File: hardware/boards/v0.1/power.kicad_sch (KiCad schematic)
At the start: 69 parts, among them IC3 SP3401-02UTG, J2 USB, U20 TPS62A02ADRLR, U23 FUSB302BxxMPX, U36 STM6601GU2BDM6F, U39 BQ27531YZFR-G1, U45 BQ24193

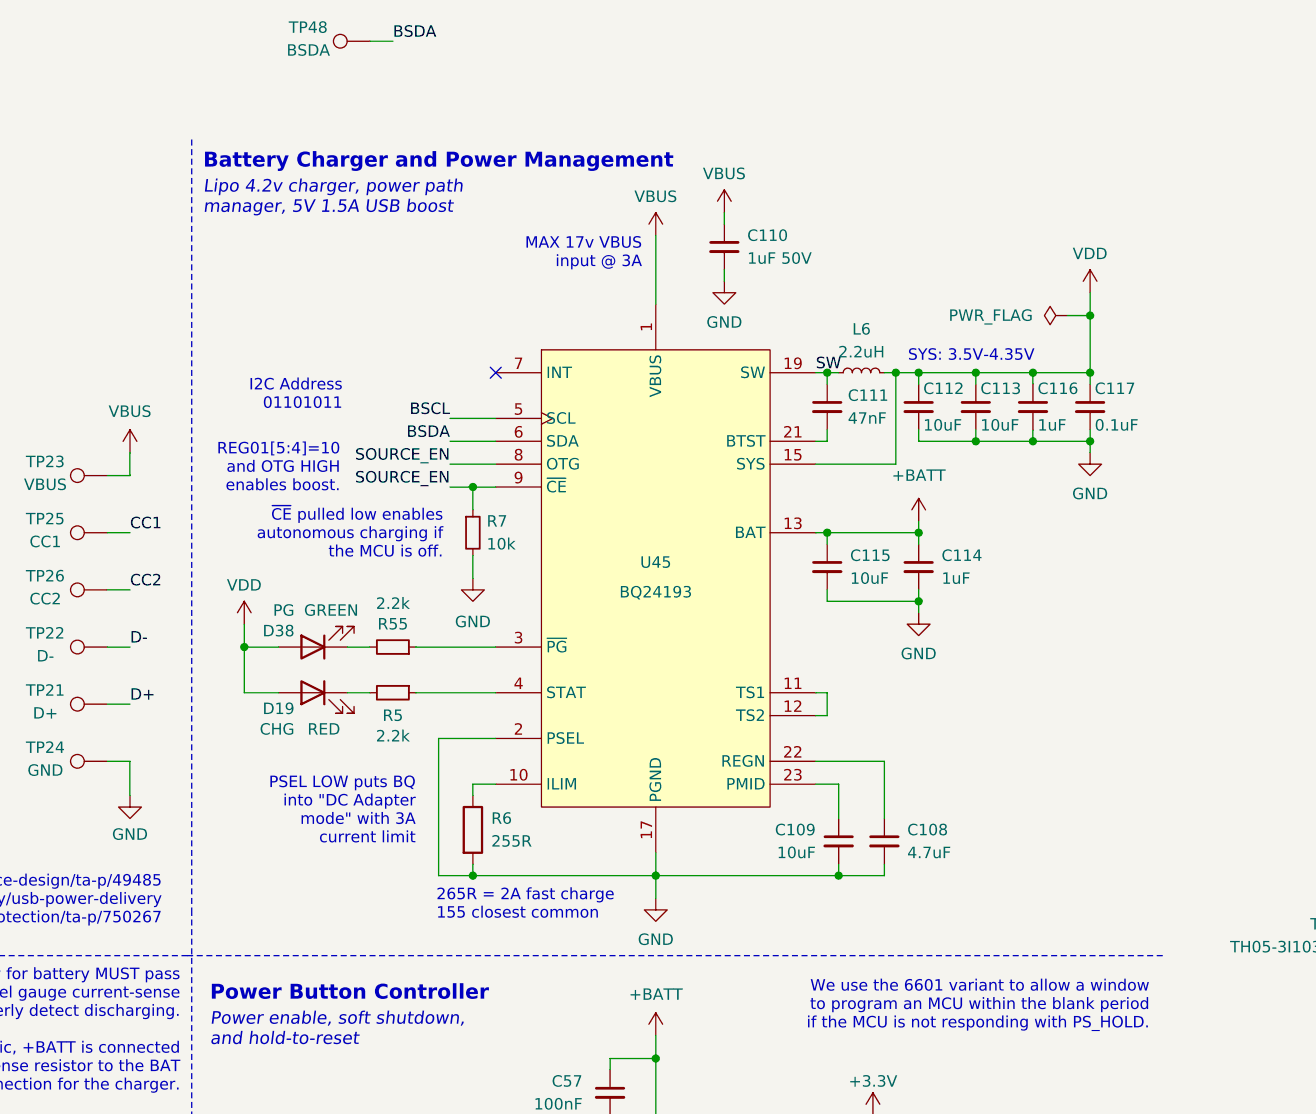
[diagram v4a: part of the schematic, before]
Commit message: chore: adjust power zone fills
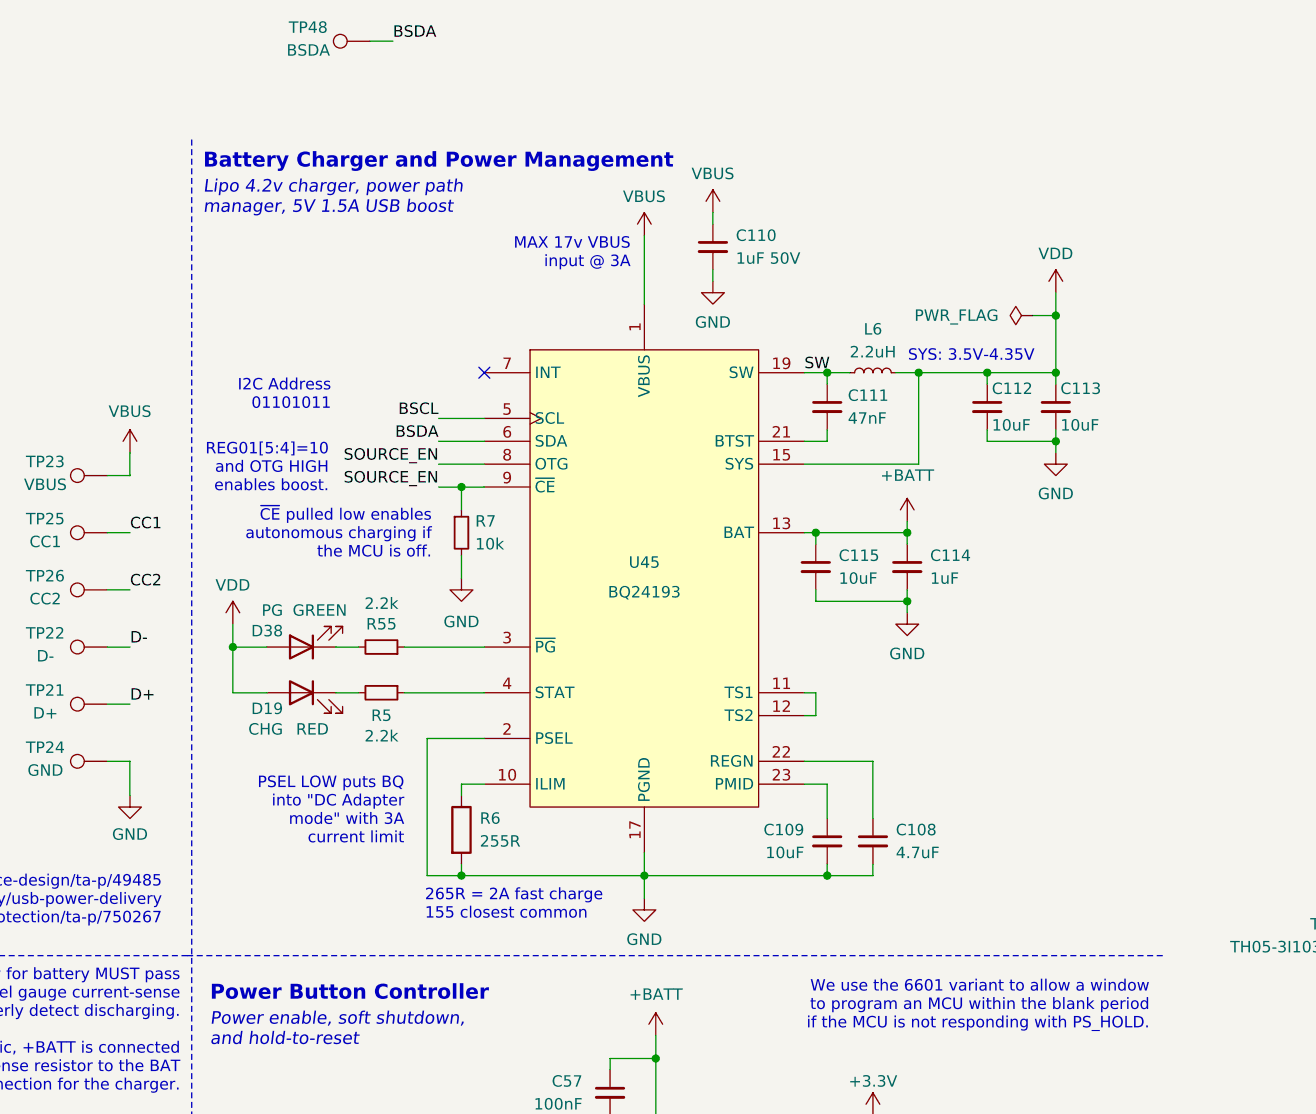
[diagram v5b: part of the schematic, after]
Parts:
- removed C116: 1uF, Capacitor_SMD:C_0402_1005Metric, symbol Device:C_Small
- removed C117: 0.1uF, Capacitor_SMD:C_0402_1005Metric, symbol Device:C_Small
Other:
- moved on the sheet: C108, C109, C110, C112, C113, C114, C115, D19, D38, L6, R5, R55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

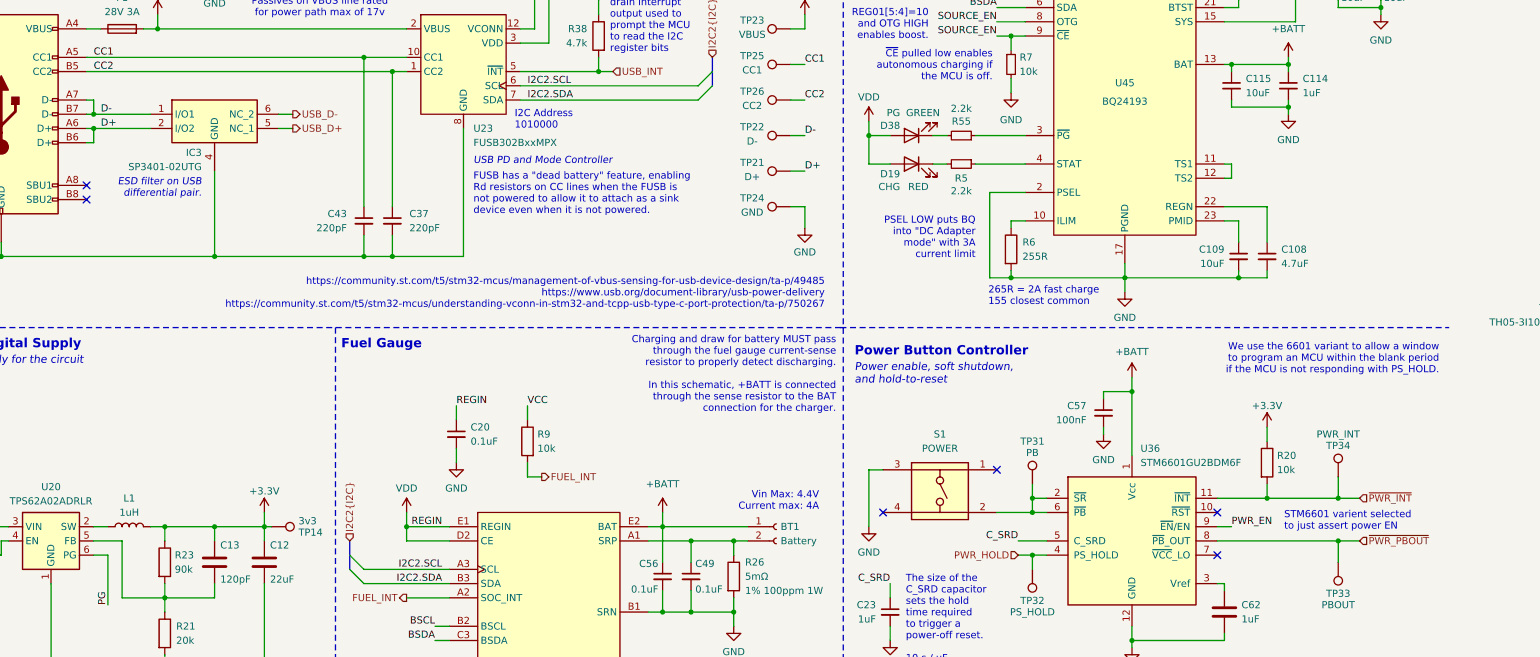
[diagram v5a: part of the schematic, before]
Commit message: chore: more power layout
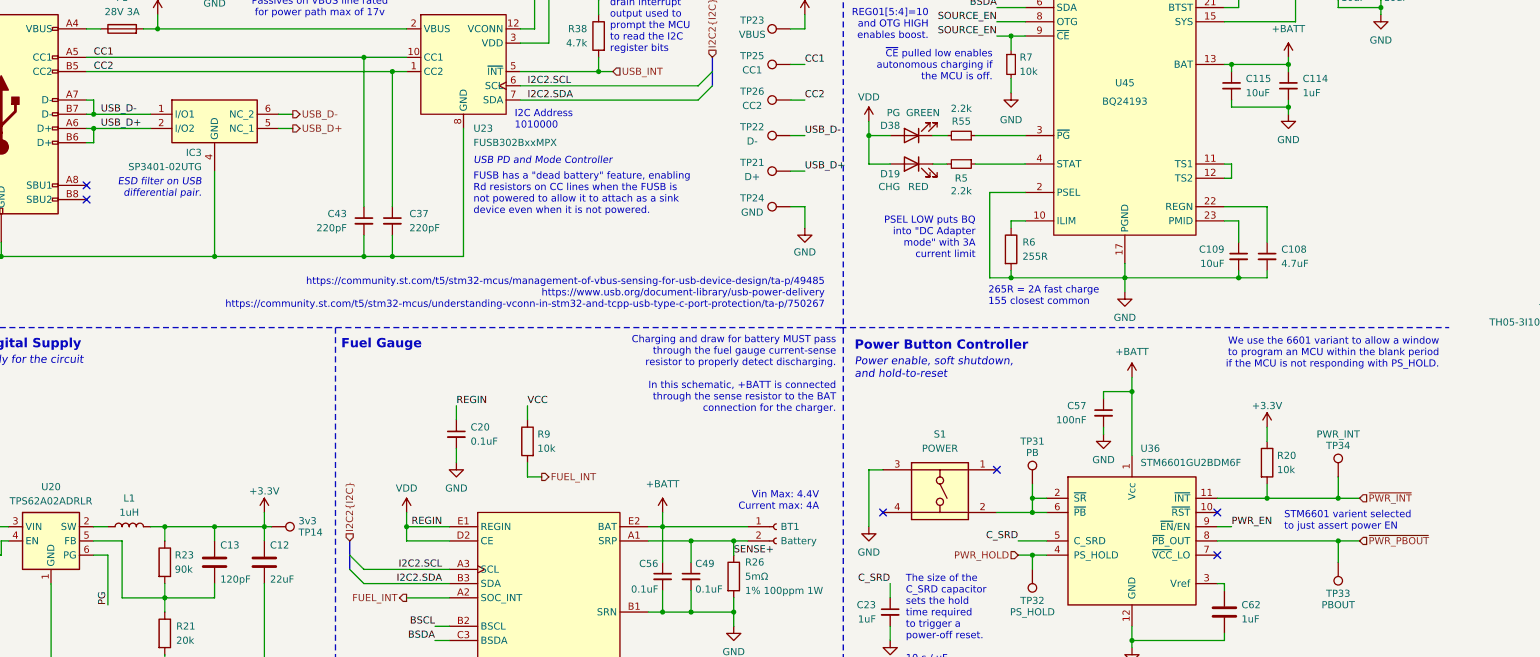
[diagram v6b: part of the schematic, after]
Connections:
- net D+ is gone; now on net USB_D+: IC3.2 (I/O2), J2.A6 (D+), J2.B6 (D+), TP21.1
- net D- is gone; now on net USB_D-: IC3.1 (I/O1), J2.A7 (D-), J2.B7 (D-), TP22.1
- net SENSE+: now reaches BT1.2 (Pin_2), C49.1, R26.1, U39.A1 (SRP)
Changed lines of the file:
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@@
 	(text "Power enable, soft shutdown,\nand hold-to-reset"
 		(exclude_from_sim no)
-		(at 179.07 109.22 0)
+		(at 179.07 108.204 0)
 		(effects
 			(font
@@
 	(text "Power Button Controller"
 		(exclude_from_sim no)
-		(at 179.07 106.172 0)
+		(at 179.07 105.156 0)
 		(effects
 			(font
@@
 	(text "We use the 6601 variant to allow a window\nto program an MCU within the blank period\nif the MCU is not responding with PS_HOLD."
 		(exclude_from_sim no)
-		(at 283.464 108.458 0)
+		(at 283.464 107.442 0)
 		(effects
 			(font
@@
 		)
 	)
-	(label "D+"
+	(label "USB_D+"
 		(at 170.18 74.93 0)
 		(effects
@@
 		)
 	)
-	(label "D-"
+	(label "USB_D-"
 		(at 44.45 64.77 0)
 		(effects
@@
 		)
 	)
-	(label "D+"
+	(label "USB_D+"
 		(at 44.45 67.31 0)
 		(effects
@@
 		)
 	)
-	(label "D-"
+	(label "USB_D-"
 		(at 170.18 68.58 0)
 		(effects
@@
 		(effects
 			(font
+				(size 1.27 1.27)
+			)
+			(justify left bottom)
+		)
+	)
+	(label "SENSE+"
+		(at 157.48 143.51 0)
+		(effects
+			(font

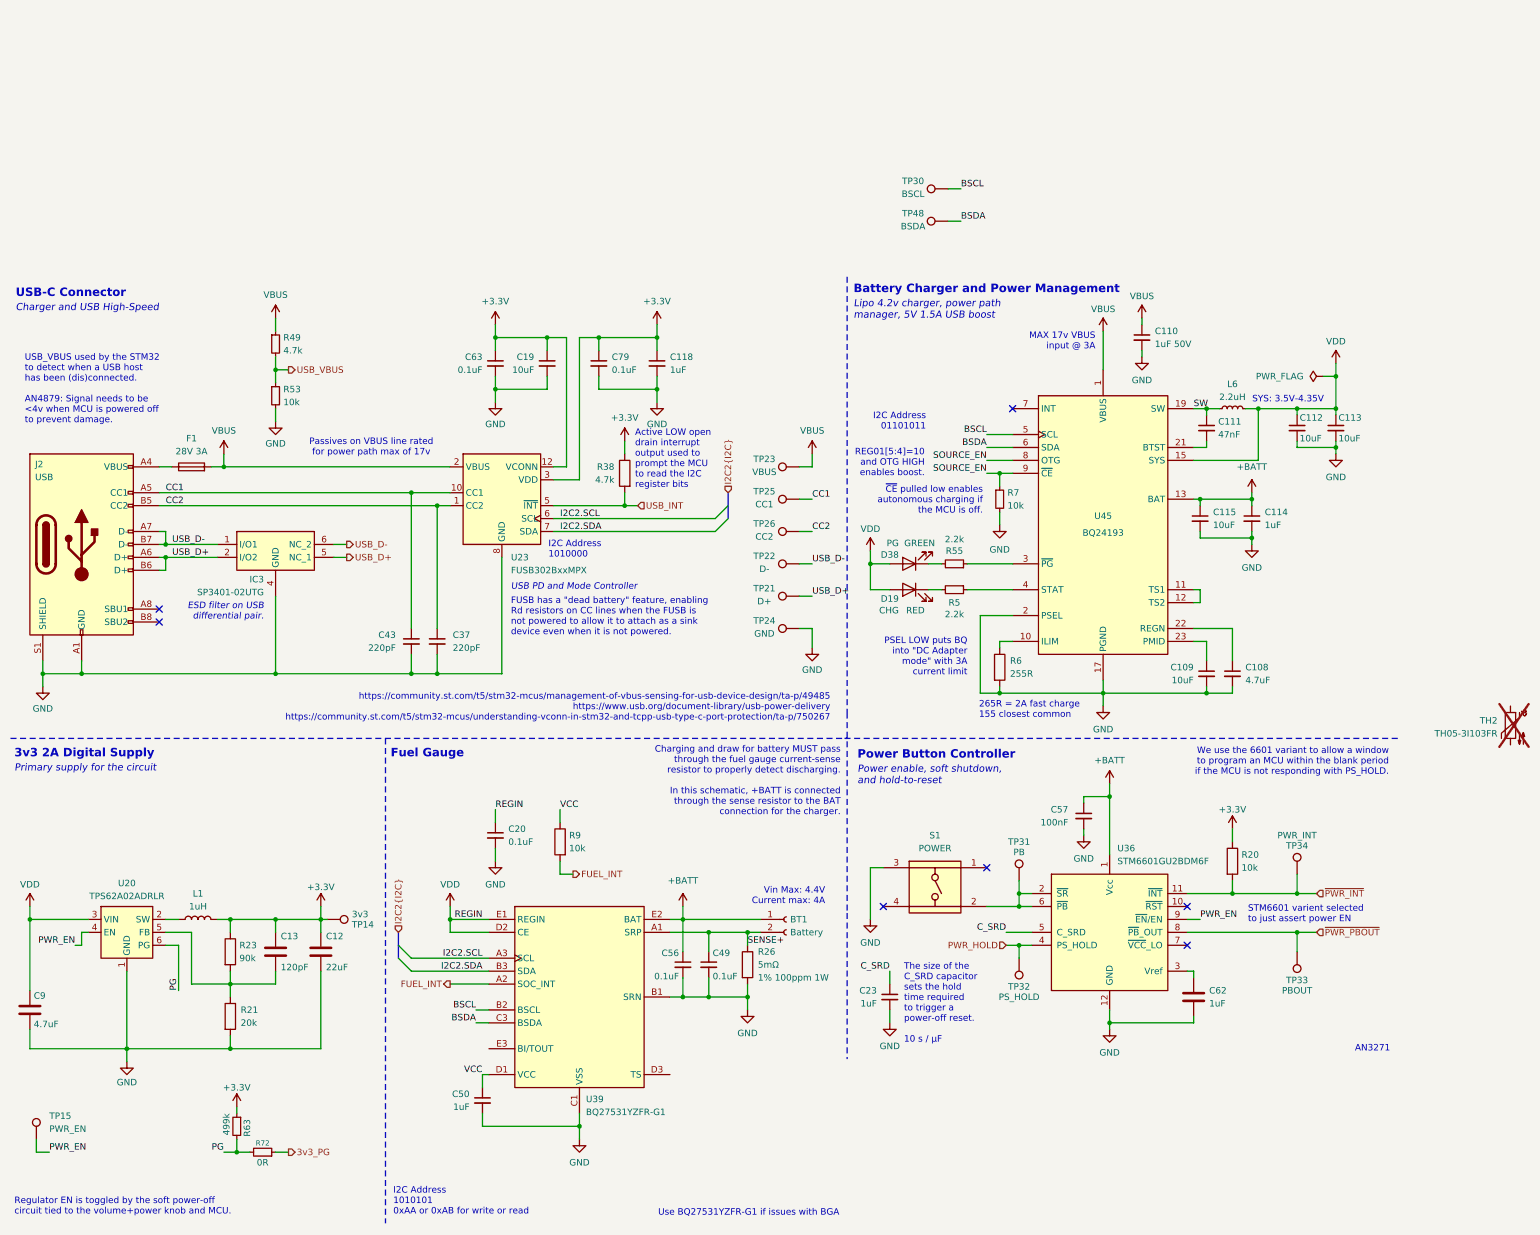
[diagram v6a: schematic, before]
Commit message: feat: finish routing new power circuit
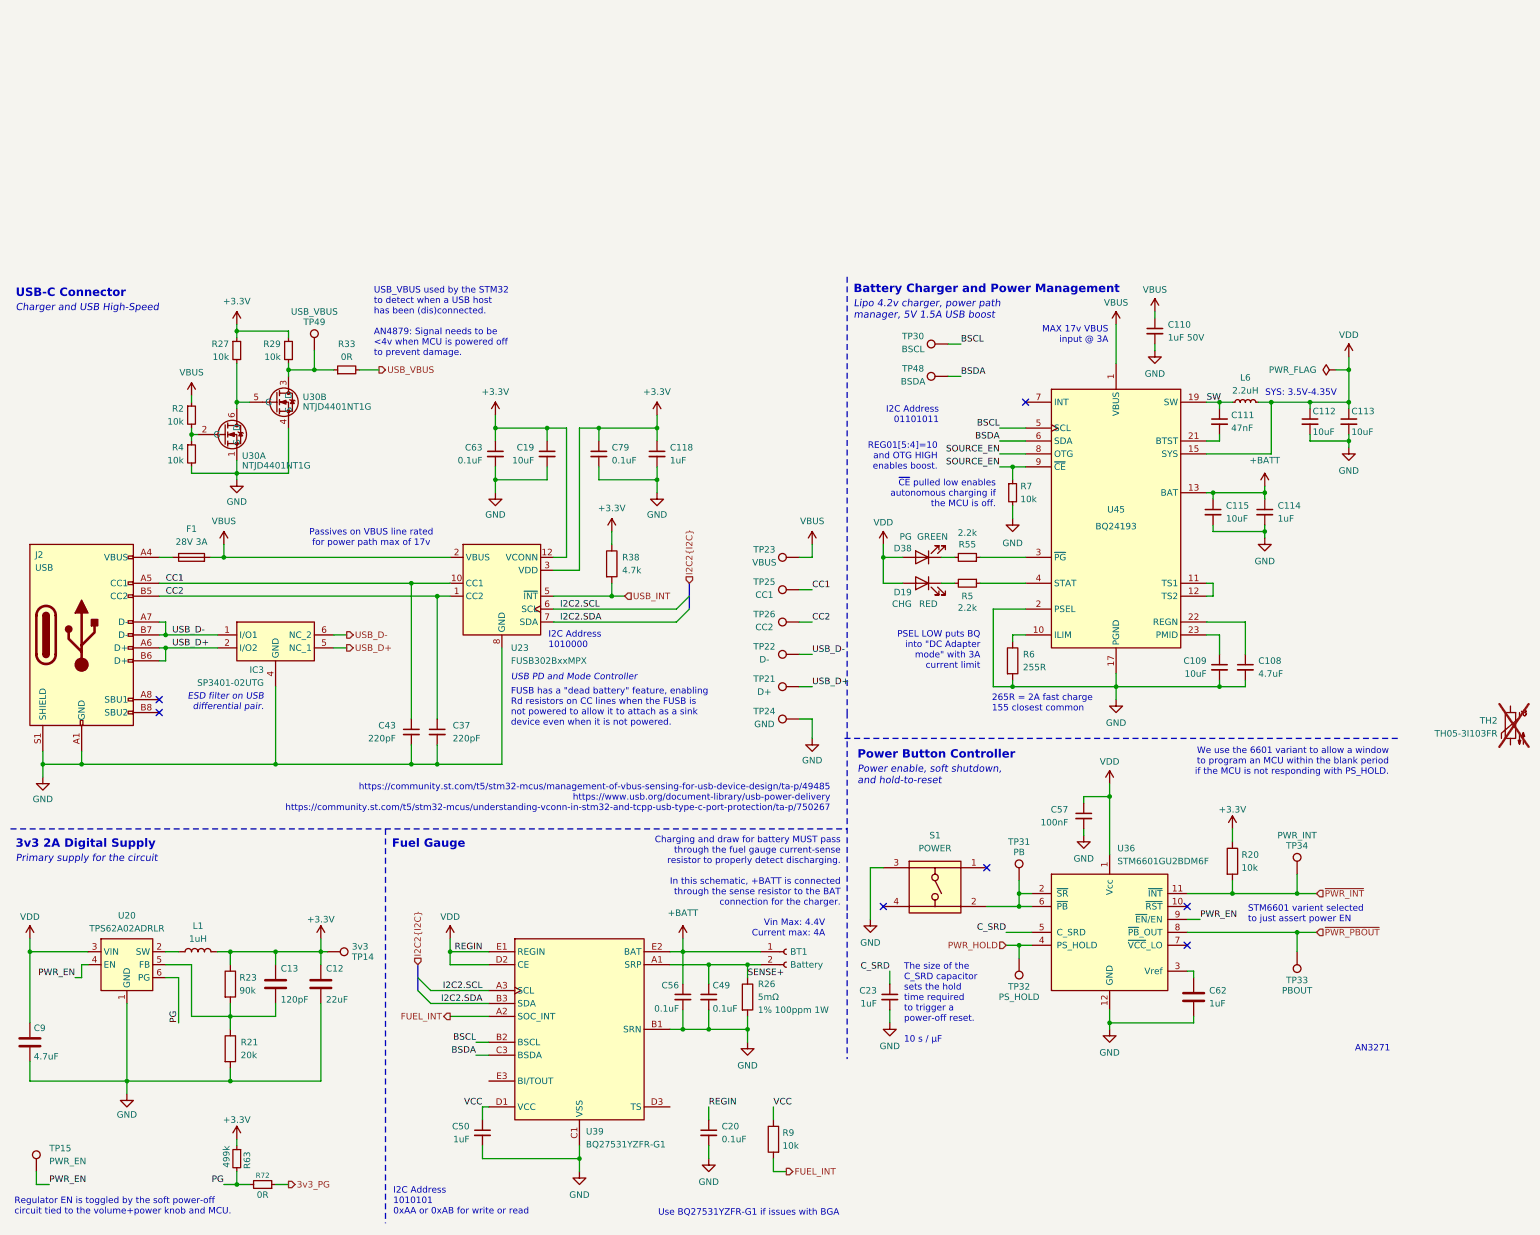
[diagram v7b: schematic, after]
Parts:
- removed R49: 4.7k, Resistor_SMD:R_0402_1005Metric, symbol Device:R_Small
- removed R53: 10k, Resistor_SMD:R_0402_1005Metric, symbol Device:R_Small
- added R2, R27, R29, R4: 10k, Resistor_SMD:R_0402_1005Metric, symbol Device:R_Small
- added R33: 0R, Resistor_SMD:R_0402_1005Metric, symbol Device:R_Small
- added TP49: USB_VBUS, TestPoint:TestPoint_Pad_D1.0mm, symbol Connector:TestPoint
- added U30: NTJD4401NT1G, Package_TO_SOT_SMD:SOT-363_SC-70-6, symbol pocket_synth:NTJD4401NT1G
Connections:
- net +3.3V: now also R27.1, R29.1
- net +BATT: no longer C57.1, U36.1 (Vcc)
- net GND: now also R4.2, U30.1 (S), U30.4 (S)
- net SYS: now also C57.1, U36.1 (Vcc)
- net USB_VBUS: now also R33.2
- net VBUS: now also R2.1
- new net: R2.2, R4.1, U30.2 (G)
- new net: R29.2, R33.1, TP49.1, U30.3 (D)
- new net: R27.2, U30.5 (G), U30.6 (D)
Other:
- note removed: "Active LOW open drain interrupt output used to prompt the MCU to read the I2C register bits"
- moved on the sheet: BT1, C108, C109, C110, C111, C112, C113, C114, C115, C118, C12, C13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
